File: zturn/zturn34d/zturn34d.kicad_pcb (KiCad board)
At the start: 4 copper layers, 59.7 x 54 mm, 26 parts, among them Q1 2N7000, U10 74AXP4T245, U11 74AXP4T245, U12 74AXP4T245, U9 74AXP4T245

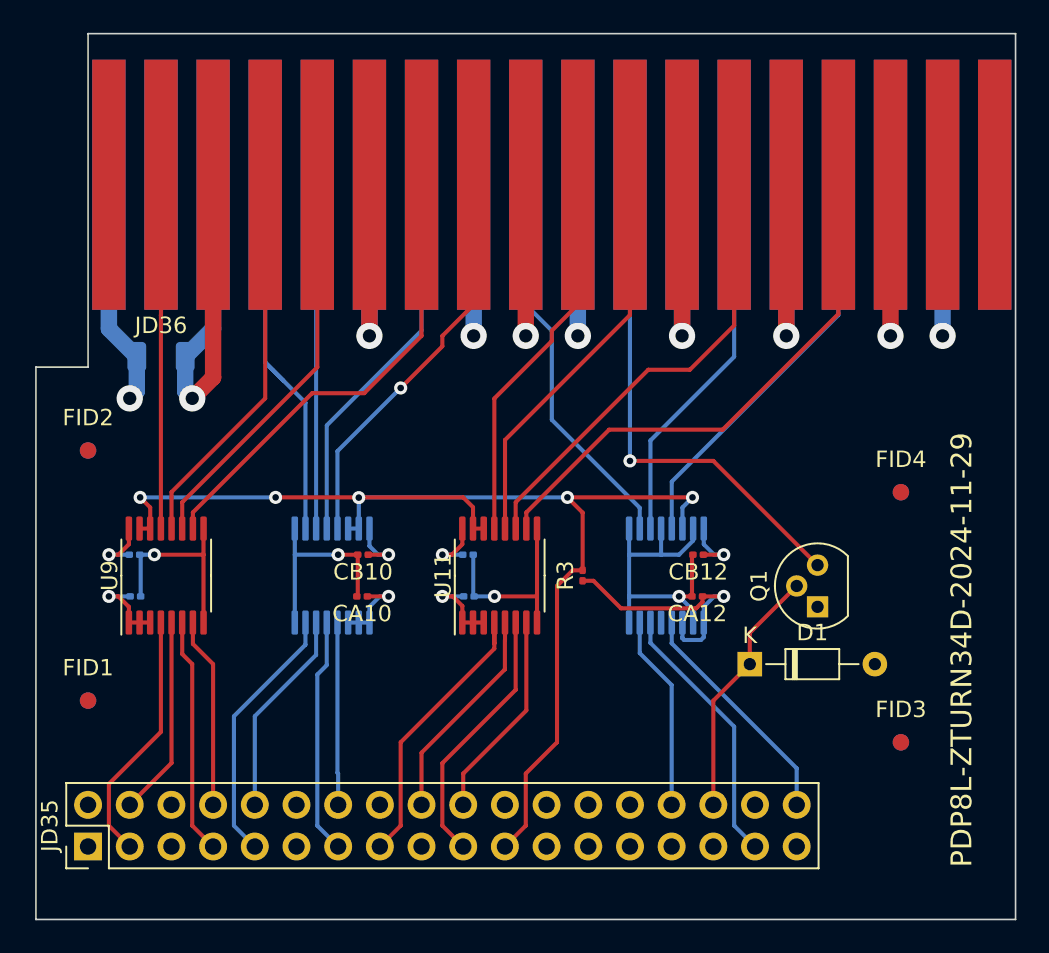
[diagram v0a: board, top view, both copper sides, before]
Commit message: use transistors for bus drivers instead of chips
to handle the 180 & 220-ohm pullups
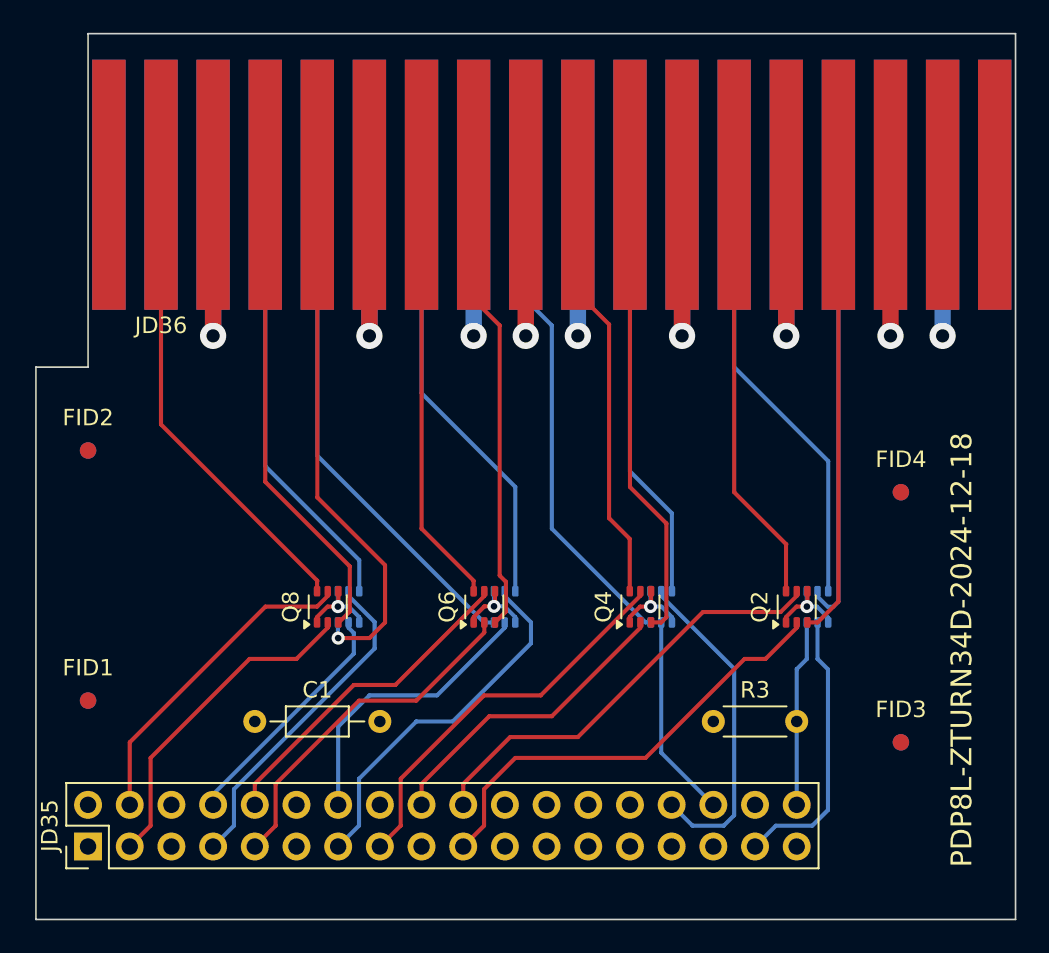
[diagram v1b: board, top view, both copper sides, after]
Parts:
- removed C3: 10u, Capacitor_SMD:C_1206_3216Metric
- removed CA10, CA11, CA12, CA9, CB10, CB11, CB12, CB9: 0.1u, Capacitor_SMD:C_0201_0603Metric
- removed D1: 5.6V, Diode_THT:D_DO-34_SOD68_P7.62mm_Horizontal
- removed U10, U11, U12, U9: 74AXP4T245, Package_SO:TSSOP-16_4.4x5mm_P0.65mm
- added C1: 0.1u, Resistor_THT:R_Axial_DIN0204_L3.6mm_D1.6mm_P7.62mm_Horizontal, F.Cu at (13.3, 41.9)
- added Q2: SSM6N15AFU, Package_TO_SOT_SMD:SOT-363_SC-70-6, F.Cu at (46.4, 34.9)
- added Q3: SSM6N15AFU, Package_TO_SOT_SMD:SOT-363_SC-70-6, B.Cu at (38.1, 34.9)
- added Q4: SSM6N15AFU, Package_TO_SOT_SMD:SOT-363_SC-70-6, F.Cu at (36.8, 34.9)
- added Q5: SSM6N15AFU, Package_TO_SOT_SMD:SOT-363_SC-70-6, B.Cu at (28.6, 34.9)
- added Q6: SSM6N15AFU, Package_TO_SOT_SMD:SOT-363_SC-70-6, F.Cu at (27.3, 34.9)
- added Q7: SSM6N15AFU, Package_TO_SOT_SMD:SOT-363_SC-70-6, B.Cu at (19.1, 34.9)
- added Q8: SSM6N15AFU, Package_TO_SOT_SMD:SOT-363_SC-70-6, F.Cu at (17.8, 34.9)
- Q1: value 2N7000 -> SSM6N15AFU; footprint Package_TO_SOT_THT:TO-92 -> Package_TO_SOT_SMD:SOT-363_SC-70-6; moved to B.Cu
- R3: value 10K -> 1K; footprint Resistor_SMD:R_0201_0603Metric -> Resistor_THT:R_Axial_DIN0204_L3.6mm_D1.6mm_P5.08mm_Horizontal
- moved R3 11.9 mm to (41.3, 41.9), turned to 0 degrees
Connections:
- Q1 pad 2: /i_INT_RQST -> /i_AC_CLEAR
- Q1 pad 3: /j_INT_RQST -> /o_B_RUN
- R3 pad 2: /_xINPUTBUS -> /o_B_RUN
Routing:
- net /_xINPUTBUS: track 74.3 -> 0.00 mm, vias 5 -> 0
- net GND: track 157.5 -> 114.4 mm
- net +5V: track 32.4 -> 0.00 mm, vias 5 -> 0
- net +3V3: track 30.6 -> 0.00 mm, vias 4 -> 0
- net /PIOBUSN: track 12.7 -> 26.6 mm
- net /j_IO_SKIP: track 16.5 -> 30.0 mm
- net /PIOBUSF: track 16.0 -> 27.5 mm
- net /jINPUTBUS_04: track 17.1 -> 27.8 mm, vias 1 -> 0
- net /jINPUTBUS_10: track 20.9 -> 31.5 mm
- net /jINPUTBUS_05: track 15.8 -> 26.1 mm
- net /jINPUTBUS_02: track 24.4 -> 32.6 mm, vias 0 -> 1
- net /i_IO_SKIP: track 11.9 -> 20.1 mm
- net /PIOBUSD: track 14.4 -> 22.4 mm
- net /jINPUTBUS_00: track 21.0 -> 28.7 mm
- net /PIOBUSH: track 12.2 -> 19.9 mm
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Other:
- board text added: "PDP8L-ZTURN34D-2024-12-18"
- board text removed: "PDP8L-ZTURN34D-2024-11-29"

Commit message: update net names on zturn pcbs to match active high/low signal type
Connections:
- net /_rBMB renamed /r_BMB
- net /_xINPUTBUS renamed /x_INPUTBUS
- net /i_INT_RQST renamed /iINT_RQST
- net /j_INT_RQST renamed /jINT_RQST
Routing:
- net /j_IO_SKIP: track 30.0 -> 23.0 mm
- net /jINPUTBUS_04: track 27.8 -> 20.8 mm
- net /jINPUTBUS_05: track 26.1 -> 19.5 mm
- net /PIOBUSJ: track 14.8 -> 14.2 mm
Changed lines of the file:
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@@
   (net 10 "/jINPUTBUS_05")
   (net 11 "/jINPUTBUS_06")
-  (net 12 "/j_INT_RQST")
+  (net 12 "/jINT_RQST")
   (net 13 "/jINPUTBUS_07")
   (net 14 "/j_AC_CLEAR")
@@
   (net 19 "unconnected-(JD36-PadT2)")
   (net 20 "unconnected-(JD36-PadV2)")
-  (net 21 "/_xINPUTBUS")
+  (net 21 "/x_INPUTBUS")
   (net 22 "unconnected-(JD36-PadU1)")
   (net 23 "unconnected-(JD36-PadV1)")
@@
   (net 37 "/PIOBUSN")
   (net 38 "unconnected-(JD35-Pin_26-Pad26)")
-  (net 39 "/_rBMB")
+  (net 39 "/r_BMB")
   (net 40 "/i_IO_SKIP")
   (net 41 "/i_AC_CLEAR")
@@
   (net 43 "unconnected-(JD36-PadB2)")
   (net 44 "+3V3")
-  (net 45 "/i_INT_RQST")
+  (net 45 "/iINT_RQST")
   (net 46 "unconnected-(JD35-Pin_35-Pad35)")
   (net 47 "unconnected-(JD36-PadA1)")
@@
       (net 37 "/PIOBUSN") (pinfunction "Pin_20") (pintype "passive"))
     (pad "21" thru_hole oval (at 0 25.4 90) (size 1.7 1.7) (drill 1) (layers "*.Cu" "*.Mask")
-      (net 21 "/_xINPUTBUS") (pinfunction "Pin_21") (pintype "passive"))
+      (net 21 "/x_INPUTBUS") (pinfunction "Pin_21") (pintype "passive"))
     (pad "22" thru_hole oval (at 2.54 25.4 90) (size 1.7 1.7) (drill 1) (layers "*.Cu" "*.Mask")
       (net 24 "unconnected-(JD35-Pin_22-Pad22)") (pinfunction "Pin_22") (pintype "passive"))
@@
       (net 17 "GND") (pinfunction "Pin_28") (pintype "passive"))
     (pad "29" thru_hole oval (at 0 35.56 90) (size 1.7 1.7) (drill 1) (layers "*.Cu" "*.Mask")
-      (net 39 "/_rBMB") (pinfunction "Pin_29") (pintype "passive"))
+      (net 39 "/r_BMB") (pinfunction "Pin_29") (pintype "passive"))
     (pad "30" thru_hole oval (at 2.54 35.56 90) (size 1.7 1.7) (drill 1) (layers "*.Cu" "*.Mask")
       (net 40 "/i_IO_SKIP") (pinfunction "Pin_30") (pintype "passive"))
@@
       (net 17 "GND") (pinfunction "Pin_31") (pintype "passive"))
     (pad "32" thru_hole oval (at 2.54 38.1 90) (size 1.7 1.7) (drill 1) (layers "*.Cu" "*.Mask")
-      (net 45 "/i_INT_RQST") (pinfunction "Pin_32") (pintype "passive"))
+      (net 45 "/iINT_RQST") (pinfunction "Pin_32") (pintype "passive"))
     (pad "33" thru_hole oval (at 0 40.64 90) (size 1.7 1.7) (drill 1) (layers "*.Cu" "*.Mask")
       (net 41 "/i_AC_CLEAR") (pinfunction "Pin_33") (pintype "passive"))
@@
       (net 11 "/jINPUTBUS_06") (pinfunction "M1") (pintype "passive"))
     (pad "M2" connect rect (at -22.225 0) (size 2.032 15.24) (layers "B.Cu" "B.Mask")
-      (net 12 "/j_INT_RQST") (pinfunction "M2") (pintype "passive"))
+      (net 12 "/jINT_RQST") (pinfunction "M2") (pintype "passive"))
     (pad "N1" connect rect (at -19.05 0) (size 2.032 15.24) (layers "F.Cu" "F.Mask")
       (net 17 "GND") (pinfunction "N1") (pintype "passive"))
@@
       (net 17 "GND") (pinfunction "S1") (pintype "passive"))
     (pad "2" smd roundrect (at -0.95 0 90) (size 0.65 0.4) (layers "B.Cu" "B.Paste" "B.Mask") (roundrect_rratio 0.25)
-      (net 45 "/i_INT_RQST") (pinfunction "G1") (pintype "passive"))
+      (net 45 "/iINT_RQST") (pinfunction "G1") (pintype "passive"))
     (pad "3" smd roundrect (at -0.95 -0.65 90) (size 0.65 0.4) (layers "B.Cu" "B.Paste" "B.Mask") (roundrect_rratio 0.25)
       (net 9 "/j_IO_SKIP") (pinfunction "D2") (pintype "passive"))
@@
       (net 40 "/i_IO_SKIP") (pinfunction "G2") (pintype "passive"))
     (pad "6" smd roundrect (at 0.95 0.65 90) (size 0.65 0.4) (layers "B.Cu" "B.Paste" "B.Mask") (roundrect_rratio 0.25)
-      (net 12 "/j_INT_RQST") (pinfunction "D1") (pintype "passive"))
+      (net 12 "/jINT_RQST") (pinfunction "D1") (pintype "passive"))
     (model "${KICAD6_3DMODEL_DIR}/Package_TO_SOT_SMD.3dshapes/SOT-363_SC-70-6.wrl"
       (offset (xyz 0 0 0))
@@
   (segment (start 13.97 27.305) (end 13.97 9.2075) (width 0.25) (layer "F.Cu") (net 2))
   (segment (start 18.460305 35.875) (end 19.125 35.210305) (width 0.25) (layer "F.Cu") (net 2))
-  (segment (start 18.43 35.875) (end 18.460305 35.875) (width 0.25) (layer "F.Cu") (net 2))
   (segment (start 19.7 32.0825) (end 19.7 33.975) (width 0.25) (layer "B.Cu") (net 3))
   (segment (start 13.97 9.2075) (end 13.97 26.3525) (width 0.25) (layer "B.Cu") (net 3))
@@
   (segment (start 29.21 27.6225) (end 23.495 21.9075) (width 0.25) (layer "B.Cu") (net 7))
   (segment (start 29.21 33.9775) (end 29.21 27.6225) (width 0.25) (layer "B.Cu") (net 7))
-  (segment (start 26.67 9.2075) (end 26.67 16.1925) (width 0.25) (layer "F.Cu") (net 8))
   (segment (start 28.2575 33.02) (end 28.635 33.3975) (width 0.25) (layer "F.Cu") (net 8))
   (segment (start 28.635 35.2125) (end 27.97 35.8775) (width 0.25) (layer "F.Cu") (net 8))
@@
   (segment (start 29.845 16.1925) (end 31.4325 17.78) (width 0.25) (layer "B.Cu") (net 9))
   (segment (start 37.1425 35.8725) (end 37.45 35.8725) (width 0.25) (layer "B.Cu") (net 9))
-  (segment (start 29.845 9.2075) (end 29.845 16.1925) (width 0.25) (layer "B.Cu") (net 9))
   (segment (start 31.4325 17.78) (end 31.4325 30.1625) (width 0.25) (layer "B.Cu") (net 9))
   (segment (start 31.4325 30.1625) (end 37.1425 35.8725) (width 0.25) (layer "B.Cu") (net 9))
-  (segment (start 33.02 15.8115) (end 33.02 9.2075) (width 0.25) (layer "F.Cu") (net 10))
   (segment (start 34.925 17.7165) (end 33.02 15.8115) (width 0.25) (layer "F.Cu") (net 10))
   (segment (start 36.18 33.9725) (end 36.18 30.7825) (width 0.25) (layer "F.Cu") (net 10))
@@
   (segment (start 37.45 34.91) (end 36.817501 34.91) (width 0.25) (layer "F.Cu") (net 17))
   (segment (start 37.48 33.9725) (end 37.48 34.88) (width 0.25) (layer "F.Cu") (net 17))
-  (segment (start 47.029999 34.91) (end 46.975 34.91) (width 0.25) (layer "F.Cu") (net 17))
   (segment (start 29.845 12.7) (end 29.845 18.415) (width 1) (layer "F.Cu") (net 17))
   (segment (start 17.13 35.550001) (end 17.13 35.875) (width 0.25) (layer "F.Cu") (net 17))
@@
   (via (at 18.4 34.91) (size 0.8) (drill 0.4) (layers "F.Cu" "B.Cu") (net 17))
   (segment (start 26.67 9.2075) (end 26.67 18.415) (width 1) (layer "B.Cu") (net 17))
-  (segment (start 46.99 34.925) (end 46.975 34.91) (width 0.25) (layer "B.Cu") (net 17))
   (segment (start 45.72 12.7) (end 45.72 18.415) (width 1) (layer "B.Cu") (net 17))
   (segment (start 37.45 34.91) (end 38.112499 34.91) (width 0.25) (layer "B.Cu") (net 17))
@@
   (segment (start 19.7 35.550001) (end 19.7 35.875) (width 0.25) (layer "B.Cu") (net 17))
   (segment (start 20.32 12.7) (end 20.32 18.415) (width 1) (layer "B.Cu") (net 17))
-  (segment (start 27.91 34.895) (end 27.94 34.925) (width 0.25) (layer "B.Cu") (net 17))
   (segment (start 47.588812 34.91) (end 48.275 35.596188) (width 0.25) (layer "B.Cu") (net 17))
   (segment (start 48.275 35.596188) (end 48.275 35.875) (width 0.25) (layer "B.Cu") (net 17))
@@
   (segment (start 33.02 9.2075) (end 33.02 18.415) (width 1) (layer "B.Cu") (net 17))
   (segment (start 19.059999 34.91) (end 19.7 35.550001) (width 0.25) (layer "B.Cu") (net 17))
-  (segment (start 37.465 34.925) (end 37.45 34.91) (width 0.25) (layer "B.Cu") (net 17))
   (segment (start 46.975 34.91) (end 47.588812 34.91) (width 0.25) (layer "B.Cu") (net 17))
   (segment (start 29.21 35.552501) (end 29.21 35.8775) (width 0.25) (layer "B.Cu") (net 17))
   (segment (start 27.91 34.895) (end 28.552499 34.895) (width 0.25) (layer "B.Cu") (net 17))
   (segment (start 38.75 35.547501) (end 38.75 35.8725) (width 0.25) (layer "B.Cu") (net 17))
-  (segment (start 18.4 34.91) (end 18.415 34.925) (width 0.25) (layer "B.Cu") (net 17))
   (segment (start 39.37 12.7) (end 39.37 18.415) (width 1) (layer "B.Cu") (net 17))
   (segment (start 38.112499 34.91) (end 38.75 35.547501) (width 0.25) (layer "B.Cu") (net 17))
@@
   (segment (start 19.3675 36.517499) (end 19.05 36.199999) (width 0.25) (layer "B.Cu") (net 29))
   (segment (start 19.3675 37.7825) (end 19.3675 36.517499) (width 0.25) (layer "B.Cu") (net 29))
-  (segment (start 10.795 46.99) (end 10.795 46.355) (width 0.25) (layer "B.Cu") (net 29))
   (segment (start 19.05 36.199999) (end 19.05 35.875) (width 0.25) (layer "B.Cu") (net 29))
   (segment (start 19.685 40.64) (end 23.1775 40.64) (width 0.25) (layer "F.Cu") (net 30))

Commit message: update software and further updates to firmware/pcbs
...for invertering transistors

./z8lsimtest works
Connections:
- net /i_AC_CLEAR renamed /iAC_CLEAR
- net /i_IO_SKIP renamed /iIO_SKIP
- net /jINT_RQST renamed /j_INT_RQST
- net /o_B_RUN renamed /oB_RUN
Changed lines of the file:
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@@
   (net 10 "/jINPUTBUS_05")
   (net 11 "/jINPUTBUS_06")
-  (net 12 "/jINT_RQST")
+  (net 12 "/j_INT_RQST")
   (net 13 "/jINPUTBUS_07")
   (net 14 "/j_AC_CLEAR")
@@
   (net 38 "unconnected-(JD35-Pin_26-Pad26)")
   (net 39 "/r_BMB")
-  (net 40 "/i_IO_SKIP")
-  (net 41 "/i_AC_CLEAR")
-  (net 42 "/o_B_RUN")
+  (net 40 "/iIO_SKIP")
+  (net 41 "/iAC_CLEAR")
+  (net 42 "/oB_RUN")
   (net 43 "unconnected-(JD36-PadB2)")
   (net 44 "+3V3")
@@
       (net 39 "/r_BMB") (pinfunction "Pin_29") (pintype "passive"))
     (pad "30" thru_hole oval (at 2.54 35.56 90) (size 1.7 1.7) (drill 1) (layers "*.Cu" "*.Mask")
-      (net 40 "/i_IO_SKIP") (pinfunction "Pin_30") (pintype "passive"))
+      (net 40 "/iIO_SKIP") (pinfunction "Pin_30") (pintype "passive"))
     (pad "31" thru_hole oval (at 0 38.1 90) (size 1.7 1.7) (drill 1) (layers "*.Cu" "*.Mask")
       (net 17 "GND") (pinfunction "Pin_31") (pintype "passive"))
@@
       (net 45 "/iINT_RQST") (pinfunction "Pin_32") (pintype "passive"))
     (pad "33" thru_hole oval (at 0 40.64 90) (size 1.7 1.7) (drill 1) (layers "*.Cu" "*.Mask")
-      (net 41 "/i_AC_CLEAR") (pinfunction "Pin_33") (pintype "passive"))
+      (net 41 "/iAC_CLEAR") (pinfunction "Pin_33") (pintype "passive"))
     (pad "34" thru_hole oval (at 2.54 40.64 90) (size 1.7 1.7) (drill 1) (layers "*.Cu" "*.Mask")
       (net 17 "GND") (pinfunction "Pin_34") (pintype "passive"))
@@
       (net 46 "unconnected-(JD35-Pin_35-Pad35)") (pinfunction "Pin_35") (pintype "passive"))
     (pad "36" thru_hole oval (at 2.54 43.18 90) (size 1.7 1.7) (drill 1) (layers "*.Cu" "*.Mask")
-      (net 42 "/o_B_RUN") (pinfunction "Pin_36") (pintype "passive"))
+      (net 42 "/oB_RUN") (pinfunction "Pin_36") (pintype "passive"))
     (model "${KICAD6_3DMODEL_DIR}/Connector_PinHeader_2.54mm.3dshapes/PinHeader_2x18_P2.54mm_Vertical.wrl"
       (offset (xyz 0 0 0))
@@
       (net 11 "/jINPUTBUS_06") (pinfunction "M1") (pintype "passive"))
     (pad "M2" connect rect (at -22.225 0) (size 2.032 15.24) (layers "B.Cu" "B.Mask")
-      (net 12 "/jINT_RQST") (pinfunction "M2") (pintype "passive"))
+      (net 12 "/j_INT_RQST") (pinfunction "M2") (pintype "passive"))
     (pad "N1" connect rect (at -19.05 0) (size 2.032 15.24) (layers "F.Cu" "F.Mask")
       (net 17 "GND") (pinfunction "N1") (pintype "passive"))
@@
       (net 44 "+3V3") (pintype "passive"))
     (pad "2" thru_hole oval (at 5.08 0) (size 1.4 1.4) (drill 0.7) (layers "*.Cu" "*.Mask")
-      (net 42 "/o_B_RUN") (pintype "passive"))
+      (net 42 "/oB_RUN") (pintype "passive"))
     (model "${KICAD6_3DMODEL_DIR}/Resistor_THT.3dshapes/R_Axial_DIN0204_L3.6mm_D1.6mm_P5.08mm_Horizontal.wrl"
       (offset (xyz 0 0 0))
@@
       (net 17 "GND") (pinfunction "S2") (pintype "passive"))
     (pad "5" smd roundrect (at 0.95 0 90) (size 0.65 0.4) (layers "B.Cu" "B.Paste" "B.Mask") (roundrect_rratio 0.25)
-      (net 40 "/i_IO_SKIP") (pinfunction "G2") (pintype "passive"))
+      (net 40 "/iIO_SKIP") (pinfunction "G2") (pintype "passive"))
     (pad "6" smd roundrect (at 0.95 0.65 90) (size 0.65 0.4) (layers "B.Cu" "B.Paste" "B.Mask") (roundrect_rratio 0.25)
-      (net 12 "/jINT_RQST") (pinfunction "D1") (pintype "passive"))
+      (net 12 "/j_INT_RQST") (pinfunction "D1") (pintype "passive"))
     (model "${KICAD6_3DMODEL_DIR}/Package_TO_SOT_SMD.3dshapes/SOT-363_SC-70-6.wrl"
       (offset (xyz 0 0 0))
@@
       (net 17 "GND") (pinfunction "S1") (pintype "passive"))
     (pad "2" smd roundrect (at -0.95 0 90) (size 0.65 0.4) (layers "B.Cu" "B.Paste" "B.Mask") (roundrect_rratio 0.25)
-      (net 41 "/i_AC_CLEAR") (pinfunction "G1") (pintype "passive"))
+      (net 41 "/iAC_CLEAR") (pinfunction "G1") (pintype "passive"))
     (pad "3" smd roundrect (at -0.95 -0.65 90) (size 0.65 0.4) (layers "B.Cu" "B.Paste" "B.Mask") (roundrect_rratio 0.25)
-      (net 42 "/o_B_RUN") (pinfunction "D2") (pintype "passive"))
+      (net 42 "/oB_RUN") (pinfunction "D2") (pintype "passive"))
     (pad "4" smd roundrect (at 0.95 -0.65 90) (size 0.65 0.4) (layers "B.Cu" "B.Paste" "B.Mask") (roundrect_rratio 0.25)
       (net 17 "GND") (pinfunction "S2") (pintype "passive"))
